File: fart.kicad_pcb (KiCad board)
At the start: 2 copper layers, 88.9 x 119.4 mm, 432 parts, among them U1 F3853, U3 74156, U4 74LS00, U5 AT28C16, X1 CartConn

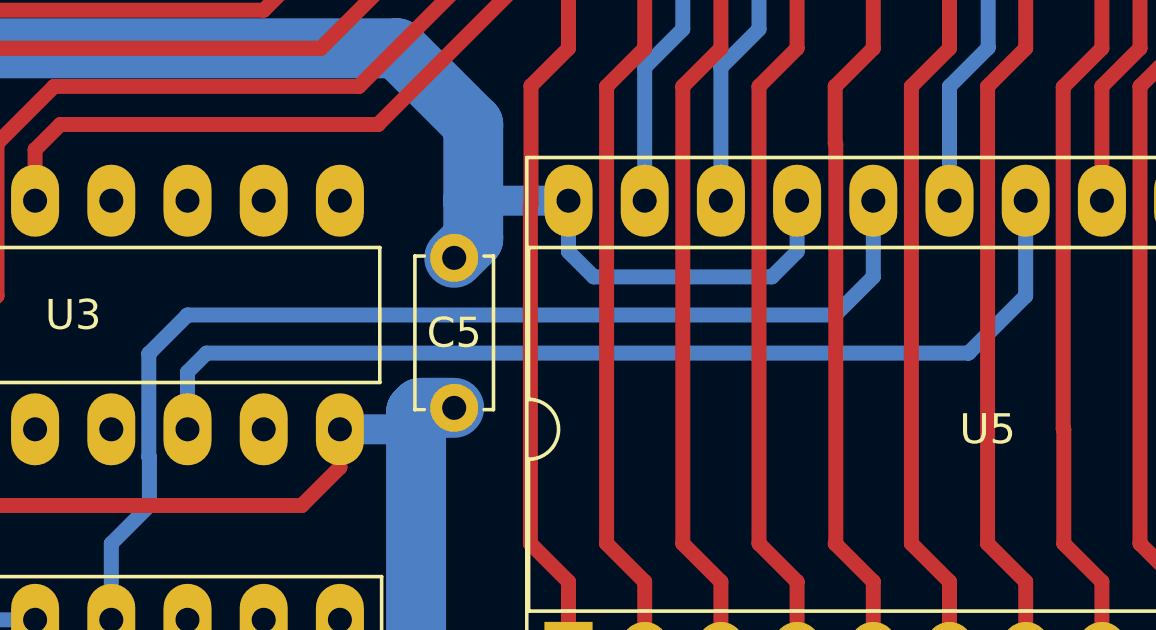
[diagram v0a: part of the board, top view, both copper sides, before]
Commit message: Fixed wrong chip select (was on 2800h instead of 0800h)
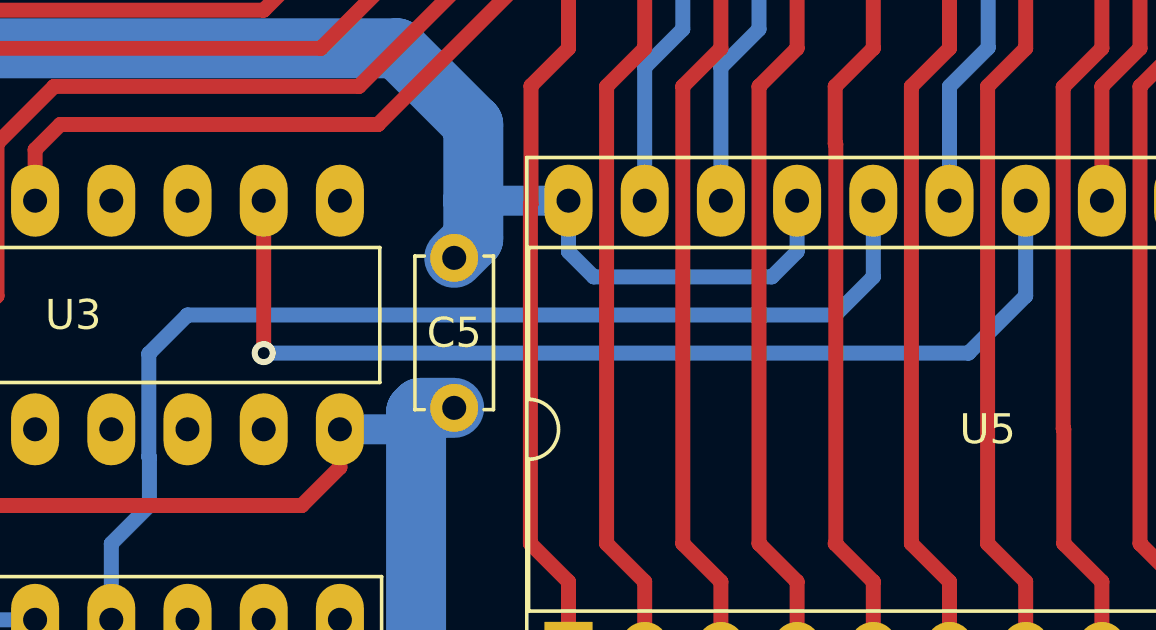
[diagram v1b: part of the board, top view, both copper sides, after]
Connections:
- U3 pad 10: /28xx -> /08xx
- U3 pad 11: /30xx -> /10xx
- U3 pad 12: /38xx -> /18xx
- U3 pad 4: /18xx -> /38xx
- U3 pad 5: /10xx -> /30xx
- U3 pad 6: /08xx -> /28xx
- U3 pad 7: /00xx -> /20xx
- U3 pad 9: /20xx -> /00xx
- U4 pad 14: +5V -> (no net)
- U4 pad 7: GND -> (no net)
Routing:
- net /08xx: track 34.1 -> 34.4 mm, vias 0 -> 1
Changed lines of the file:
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@@
   )
   (setup
-    (last_trace_width 0.25)
+    (last_trace_width 0.5)
     (user_trace_width 0.5)
     (user_trace_width 1)
@@
     (pad 13 thru_hole oval (at 7.62 2.54 90) (size 2.4 1.6) (drill 0.8) (layers *.Cu *.Mask)
       (net 39 /CPU_READ))
-    (pad 7 thru_hole oval (at 0 15.24 90) (size 2.4 1.6) (drill 0.8) (layers *.Cu *.Mask)
-      (net 2 GND))
-    (pad 14 thru_hole oval (at 7.62 0 90) (size 2.4 1.6) (drill 0.8) (layers *.Cu *.Mask)
-      (net 1 +5V))
+    (pad 7 thru_hole oval (at 0 15.24 90) (size 2.4 1.6) (drill 0.8) (layers *.Cu *.Mask))
+    (pad 14 thru_hole oval (at 7.62 0 90) (size 2.4 1.6) (drill 0.8) (layers *.Cu *.Mask))
     (model ${KISYS3DMOD}/Housings_DIP.3dshapes/DIP-14_W7.62mm_Socket.wrl
       (at (xyz 0 0 0))
@@
       (net 31 /A13))
     (pad 7 thru_hole oval (at 0 15.24 90) (size 2.4 1.6) (drill 0.8) (layers *.Cu *.Mask)
-      (net 41 /00xx))
+      (net 48 /20xx))
     (pad 14 thru_hole oval (at 7.62 5.08 90) (size 2.4 1.6) (drill 0.8) (layers *.Cu *.Mask)
       (net 2 GND))
     (pad 6 thru_hole oval (at 0 12.7 90) (size 2.4 1.6) (drill 0.8) (layers *.Cu *.Mask)
-      (net 42 /08xx))
+      (net 47 /28xx))
     (pad 13 thru_hole oval (at 7.62 7.62 90) (size 2.4 1.6) (drill 0.8) (layers *.Cu *.Mask)
       (net 27 /A11))
     (pad 5 thru_hole oval (at 0 10.16 90) (size 2.4 1.6) (drill 0.8) (layers *.Cu *.Mask)
-      (net 43 /10xx))
+      (net 46 /30xx))
     (pad 12 thru_hole oval (at 7.62 10.16 90) (size 2.4 1.6) (drill 0.8) (layers *.Cu *.Mask)
-      (net 44 /38xx))
-    (pad 4 thru_hole oval (at 0 7.62 90) (size 2.4 1.6) (drill 0.8) (layers *.Cu *.Mask)
       (net 45 /18xx))
+    (pad 4 thru_hole oval (at 0 7.62 90) (size 2.4 1.6) (drill 0.8) (layers *.Cu *.Mask)
+      (net 44 /38xx))
     (pad 11 thru_hole oval (at 7.62 12.7 90) (size 2.4 1.6) (drill 0.8) (layers *.Cu *.Mask)
-      (net 46 /30xx))
+      (net 43 /10xx))
     (pad 3 thru_hole oval (at 0 5.08 90) (size 2.4 1.6) (drill 0.8) (layers *.Cu *.Mask)
       (net 29 /A12))
     (pad 10 thru_hole oval (at 7.62 15.24 90) (size 2.4 1.6) (drill 0.8) (layers *.Cu *.Mask)
-      (net 47 /28xx))
+      (net 42 /08xx))
     (pad 2 thru_hole oval (at 0 2.54 90) (size 2.4 1.6) (drill 0.8) (layers *.Cu *.Mask)
       (net 2 GND))
     (pad 9 thru_hole oval (at 7.62 17.78 90) (size 2.4 1.6) (drill 0.8) (layers *.Cu *.Mask)
-      (net 48 /20xx))
+      (net 41 /00xx))
     (pad 1 thru_hole rect (at 0 0 90) (size 2.4 1.6) (drill 0.8) (layers *.Cu *.Mask)
       (net 31 /A13))
@@
   (segment (start 161.29 75.565) (end 161.29 76.835) (width 0.5) (layer B.Cu) (net 18))
   (segment (start 161.29 76.835) (end 164.465 80.01) (width 0.5) (layer B.Cu) (net 18))
+  (via (at 134.62 124.46) (size 0.8) (drill 0.4) (layers F.Cu B.Cu) (net 42))
   (via (at 156.21 75.565) (size 0.8) (drill 0.4) (layers F.Cu B.Cu) (net 19))
   (segment (start 156.21 69.215) (end 156.21 75.565) (width 0.5) (layer B.Cu) (net 19))
@@
   (segment (start 161.29 127) (end 161.29 130.81) (width 0.5) (layer F.Cu) (net 40))
   (segment (start 160.02 122.555) (end 160.02 119.38) (width 0.5) (layer B.Cu) (net 42))
+  (segment (start 134.62 124.46) (end 158.115 124.46) (width 0.5) (layer B.Cu) (net 42))
   (segment (start 158.115 124.46) (end 160.02 122.555) (width 0.5) (layer B.Cu) (net 42))
-  (segment (start 132.08 127) (end 132.08 125.095) (width 0.5) (layer B.Cu) (net 42))
-  (segment (start 132.715 124.46) (end 158.115 124.46) (width 0.5) (layer B.Cu) (net 42))
-  (segment (start 132.08 125.095) (end 132.715 124.46) (width 0.5) (layer B.Cu) (net 42))
+  (segment (start 134.62 119.38) (end 134.62 124.46) (width 0.5) (layer F.Cu) (net 42))
   (segment (start 130.81 129.54) (end 129.54 130.81) (width 0.5) (layer B.Cu) (net 49))
   (segment (start 154.94 121.92) (end 153.67 123.19) (width 0.5) (layer B.Cu) (net 49))
